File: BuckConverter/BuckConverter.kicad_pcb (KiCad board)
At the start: 2 copper layers, 130.3 x 135.9 mm, 43 parts, among them J1 Conn_01x01_Pin, J2 Conn_01x01_Pin, J3 Conn_01x01_Pin, J4 Conn_01x01_Pin, J5 Conn_01x01_Pin, Q1 IRF540N, U1 LM358, U2 LAUNCHXL-F28379D, U3 UCC5304DWVR, U4 TMV 0512SHI

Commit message: LPF updates
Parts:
- R1: value 10000 -> 10k
- R2, R3: value ? -> 500; footprint Resistor_SMD:R_0805_2012Metric -> Resistor_SMD:R_0603_1608Metric
- R4: value ? -> 10k
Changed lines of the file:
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@@
 		(tags "resistor")
 		(property "Reference" "R4"
-			(at 2.794 0 0)
+			(at 0 -1.65 180)
 			(layer "F.SilkS")
 			(effects
@@
 			)
 		)
-		(property "Value" "?"
-			(at 0 1.65 0)
+		(property "Value" "10k"
+			(at 0 1.65 180)
 			(layer "F.Fab")
 			(effects
@@
 		)
 		(fp_text user "${REFERENCE}"
-			(at 0 0 0)
+			(at 0 0 180)
 			(layer "F.Fab")
 			(effects
@@
 			)
 		)
-		(property "Value" "10000"
+		(property "Value" "10k"
 			(at 0 1.65 0)
 			(layer "F.Fab")
@@
 		)
 	)
-	(footprint "Resistor_SMD:R_0805_2012Metric"
+	(footprint "Resistor_SMD:R_0603_1608Metric"
 		(layer "F.Cu")
 		(at 147.392 112.756)
-		(descr "Resistor SMD 0805 (2012 Metric), square (rectangular) end terminal, IPC_7351 nominal, (Body size source: IPC-SM-782 page 72, https://www.pcb-3d.com/wordpress/wp-content/uploads/ipc-sm-782a_amendment_1_and_2.pdf), generated with kicad-footprint-generator")
+		(descr "Resistor SMD 0603 (1608 Metric), square (rectangular) end terminal, IPC_7351 nominal, (Body size source: IPC-SM-782 page 72, https://www.pcb-3d.com/wordpress/wp-content/uploads/ipc-sm-782a_amendment_1_and_2.pdf), generated with kicad-footprint-generator")
 		(tags "resistor")
 		(property "Reference" "R2"
-			(at 2.794 0 0)
+			(at 0 -1.43 0)
 			(layer "F.SilkS")
 			(effects
@@
 			)
 		)
-		(property "Value" "?"
-			(at 0 1.65 0)
+		(property "Value" "500"
+			(at 0 1.43 0)
 			(layer "F.Fab")
 			(effects
@@
 			)
 		)
-		(property "Footprint" "Resistor_SMD:R_0805_2012Metric"
+		(property "Footprint" "Resistor_SMD:R_0603_1608Metric"
 			(at 0 0 0)
 			(unlocked yes)
@@
 			)
 		)
-		(property "Part Number" "RMCF0805FT10K0"
+		(property "Part Number" "RT0603BRC07500RL"
 			(at 0 0 0)
 			(unlocked yes)
@@
 		(attr smd)
 		(fp_line
-			(start -0.227064 -0.735)
-			(end 0.227064 -0.735)
+			(start -0.237258 -0.5225)
+			(end 0.237258 -0.5225)
 			(stroke
 				(width 0.12)
@@
 		)
 		(fp_line
-			(start -0.227064 0.735)
-			(end 0.227064 0.735)
+			(start -0.237258 0.5225)
+			(end 0.237258 0.5225)
 			(stroke
 				(width 0.12)
@@
 		)
 		(fp_line
-			(start -1.68 -0.95)
-			(end 1.68 -0.95)
+			(start -1.48 -0.73)
+			(end 1.48 -0.73)
 			(stroke
 				(width 0.05)
@@
 		)
 		(fp_line
-			(start -1.68 0.95)
-			(end -1.68 -0.95)
+			(start -1.48 0.73)
+			(end -1.48 -0.73)
 			(stroke
 				(width 0.05)
@@
 		)
 		(fp_line
-			(start 1.68 -0.95)
-			(end 1.68 0.95)
+			(start 1.48 -0.73)
+			(end 1.48 0.73)
 			(stroke
 				(width 0.05)
@@
 		)
 		(fp_line
-			(start 1.68 0.95)
-			(end -1.68 0.95)
+			(start 1.48 0.73)
+			(end -1.48 0.73)
 			(stroke
 				(width 0.05)
@@
 		)
 		(fp_line
-			(start -1 -0.625)
-			(end 1 -0.625)
+			(start -0.8 -0.4125)
+			(end 0.8 -0.4125)
 			(stroke
 				(width 0.1)
@@
 		)
 		(fp_line
-			(start -1 0.625)
-			(end -1 -0.625)
+			(start -0.8 0.4125)
+			(end -0.8 -0.4125)
 			(stroke
 				(width 0.1)
@@
 		)
 		(fp_line
-			(start 1 -0.625)
-			(end 1 0.625)
+			(start 0.8 -0.4125)
+			(end 0.8 0.4125)
 			(stroke
 				(width 0.1)
@@
 		)
 		(fp_line
-			(start 1 0.625)
-			(end -1 0.625)
+			(start 0.8 0.4125)
+			(end -0.8 0.4125)
 			(stroke
 				(width 0.1)
@@
 			(effects
 				(font
-					(size 0.5 0.5)
-					(thickness 0.08)
+					(size 0.4 0.4)
+					(thickness 0.06)
 				)
 			)
 		)
 		(pad "1" smd roundrect
-			(at -0.9125 0)
-			(size 1.025 1.4)
+			(at -0.825 0)
+			(size 0.8 0.95)
 			(layers "F.Cu" "F.Paste" "F.Mask")
-			(roundrect_rratio 0.243902)
+			(roundrect_rratio 0.25)
 			(net 2 "Net-(U1A--)")
 			(pintype "passive")
 		)
 		(pad "2" smd roundrect
-			(at 0.9125 0)
-			(size 1.025 1.4)
+			(at 0.825 0)
+			(size 0.8 0.95)
 			(layers "F.Cu" "F.Paste" "F.Mask")
-			(roundrect_rratio 0.243902)
+			(roundrect_rratio 0.25)
 			(net 6 "/LPF/VFLIT")
 			(pintype "passive")
 		)
-		(model "${KICAD8_3DMODEL_DIR}/Resistor_SMD.3dshapes/R_0805_2012Metric.wrl"
+		(model "${KICAD8_3DMODEL_DIR}/Resistor_SMD.3dshapes/R_0603_1608Metric.wrl"
 			(offset
 				(xyz 0 0 0)
@@
 			)
 		)
-		(fp_text user "*"
-			(at -3.4163 -2.8956 0)
+		(fp_text user "${REFERENCE}"
+			(at 0 0 0)
+			(unlocked yes)
 			(layer "F.Fab")
 			(effects
@@
 			)
 		)
-		(fp_text user "${REFERENCE}"
-			(at 0 0 0)
-			(unlocked yes)
+		(fp_text user "*"
+			(at -3.4163 -2.8956 0)
 			(layer "F.Fab")
 			(effects
@@
 		(fp_text user "*"
 			(at -3.1196 0 0)
+			(unlocked yes)
 			(layer "F.SilkS")
 			(effects
@@
 		(fp_text user "*"
 			(at -3.1196 0 0)
-			(unlocked yes)
 			(layer "F.SilkS")
 			(effects
@@
 		(fp_text user "*"
 			(at -1.8496 0 0)
+			(unlocked yes)
 			(layer "F.Fab")
 			(effects
@@
 			)
 		)
-		(fp_text user "${REFERENCE}"
-			(at 7.65 2.075 0)
-			(unlocked yes)
+		(fp_text user "*"
+			(at -1.8496 0 0)
 			(layer "F.Fab")
 			(effects
@@
 			)
 		)
-		(fp_text user "*"
-			(at -1.8496 0 0)
+		(fp_text user "${REFERENCE}"
+			(at 7.65 2.075 0)
 			(unlocked yes)
 			(layer "F.Fab")
@@
 		)
 	)
-	(footprint "Resistor_SMD:R_0805_2012Metric"
+	(footprint "Resistor_SMD:R_0603_1608Metric"
 		(layer "F.Cu")
 		(at 147.392 105.898)
-		(descr "Resistor SMD 0805 (2012 Metric), square (rectangular) end terminal, IPC_7351 nominal, (Body size source: IPC-SM-782 page 72, https://www.pcb-3d.com/wordpress/wp-content/uploads/ipc-sm-782a_amendment_1_and_2.pdf), generated with kicad-footprint-generator")
+		(descr "Resistor SMD 0603 (1608 Metric), square (rectangular) end terminal, IPC_7351 nominal, (Body size source: IPC-SM-782 page 72, https://www.pcb-3d.com/wordpress/wp-content/uploads/ipc-sm-782a_amendment_1_and_2.pdf), generated with kicad-footprint-generator")
 		(tags "resistor")
 		(property "Reference" "R3"
-			(at 2.794 0 0)
+			(at 0 -1.43 0)
 			(layer "F.SilkS")
 			(effects
@@
 			)
 		)
-		(property "Value" "?"
-			(at 0 1.65 0)
+		(property "Value" "500"
+			(at 0 1.43 0)
 			(layer "F.Fab")
 			(effects
@@
 			)
 		)
-		(property "Footprint" "Resistor_SMD:R_0805_2012Metric"
+		(property "Footprint" "Resistor_SMD:R_0603_1608Metric"
 			(at 0 0 0)
 			(unlocked yes)
@@
 			)
 		)
-		(property "Part Number" "RMCF0805FT10K0"
+		(property "Part Number" "RT0603BRC07500RL"
 			(at 0 0 0)
 			(unlocked yes)
@@
 		(attr smd)
 		(fp_line
-			(start -0.227064 -0.735)
-			(end 0.227064 -0.735)
+			(start -0.237258 -0.5225)
+			(end 0.237258 -0.5225)
 			(stroke
 				(width 0.12)
@@
 		)
 		(fp_line
-			(start -0.227064 0.735)
-			(end 0.227064 0.735)
+			(start -0.237258 0.5225)
+			(end 0.237258 0.5225)
 			(stroke
 				(width 0.12)
@@
 		)
 		(fp_line
-			(start -1.68 -0.95)
-			(end 1.68 -0.95)
+			(start -1.48 -0.73)
+			(end 1.48 -0.73)
 			(stroke
 				(width 0.05)
@@
 		)
 		(fp_line
-			(start -1.68 0.95)
-			(end -1.68 -0.95)
+			(start -1.48 0.73)
+			(end -1.48 -0.73)
 			(stroke
 				(width 0.05)
@@
 		)
 		(fp_line
-			(start 1.68 -0.95)
-			(end 1.68 0.95)
+			(start 1.48 -0.73)
+			(end 1.48 0.73)
 			(stroke
 				(width 0.05)
@@
 		)
 		(fp_line
-			(start 1.68 0.95)
-			(end -1.68 0.95)
+			(start 1.48 0.73)
+			(end -1.48 0.73)
 			(stroke
 				(width 0.05)
@@
 		)
 		(fp_line
-			(start -1 -0.625)
-			(end 1 -0.625)
+			(start -0.8 -0.4125)
+			(end 0.8 -0.4125)
 			(stroke
 				(width 0.1)
@@
 		)
 		(fp_line
-			(start -1 0.625)
-			(end -1 -0.625)
+			(start -0.8 0.4125)
+			(end -0.8 -0.4125)
 			(stroke
 				(width 0.1)
@@
 		)
 		(fp_line
-			(start 1 -0.625)
-			(end 1 0.625)
+			(start 0.8 -0.4125)
+			(end 0.8 0.4125)
 			(stroke
 				(width 0.1)
@@
 		)
 		(fp_line
-			(start 1 0.625)
-			(end -1 0.625)
+			(start 0.8 0.4125)
+			(end -0.8 0.4125)
 			(stroke
 				(width 0.1)
@@
 			(effects
 				(font
-					(size 0.5 0.5)
-					(thickness 0.08)
+					(size 0.4 0.4)
+					(thickness 0.06)
 				)
 			)
 		)
 		(pad "1" smd roundrect
-			(at -0.9125 0)
-			(size 1.025 1.4)
+			(at -0.825 0)
+			(size 0.8 0.95)
 			(layers "F.Cu" "F.Paste" "F.Mask")
-			(roundrect_rratio 0.243902)
+			(roundrect_rratio 0.25)
 			(net 4 "Net-(U1A-+)")
 			(pintype "passive")
 		)
 		(pad "2" smd roundrect
-			(at 0.9125 0)
-			(size 1.025 1.4)
+			(at 0.825 0)
+			(size 0.8 0.95)
 			(layers "F.Cu" "F.Paste" "F.Mask")
-			(roundrect_rratio 0.243902)
+			(roundrect_rratio 0.25)
 			(net 1 "GND")
 			(pintype "passive")
 		)
-		(model "${KICAD8_3DMODEL_DIR}/Resistor_SMD.3dshapes/R_0805_2012Metric.wrl"
+		(model "${KICAD8_3DMODEL_DIR}/Resistor_SMD.3dshapes/R_0603_1608Metric.wrl"
 			(offset
 				(xyz 0 0 0)

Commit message: pcb name printed
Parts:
- added G***: LOGO, uwinengineeringlogo:uwinengilogo, F.Cu at (54.0, 59.9)
- added G***: LOGO, Totoro:Totoro, F.Cu at (63.2, 67.6)
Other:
- board text added: "Studio Buck Converter v0 - 24 Feb 2025 Steven Fung Andrew Nguyen Yanis Belassel"

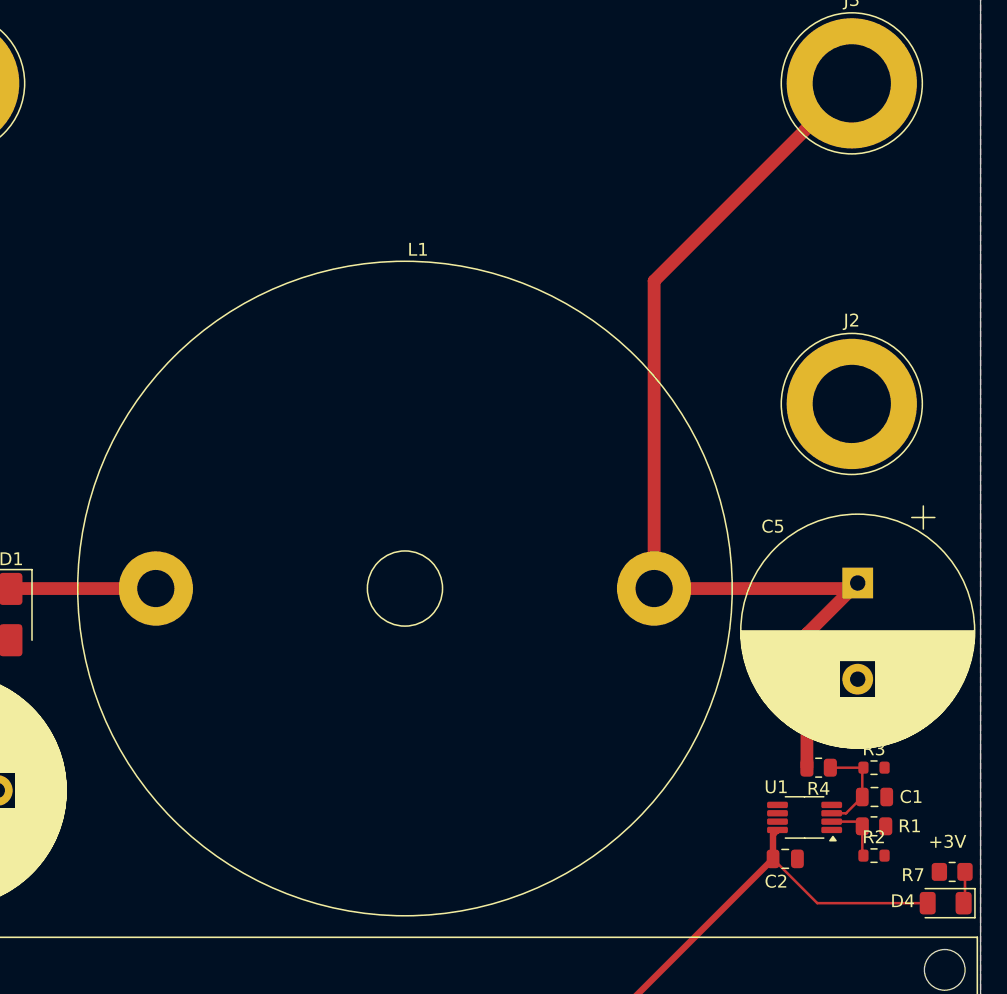
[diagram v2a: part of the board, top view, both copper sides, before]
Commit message: PCB updated LC footprints
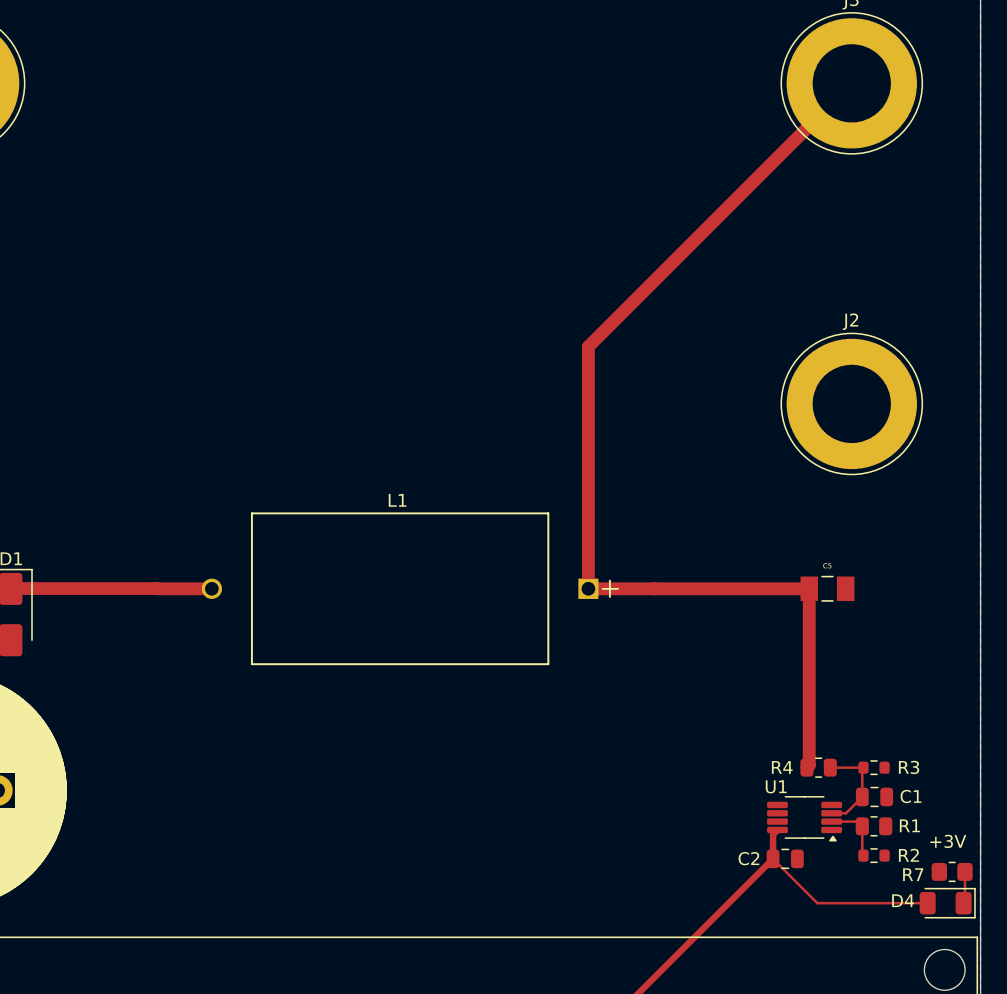
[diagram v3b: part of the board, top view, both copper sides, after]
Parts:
- C1: value C -> 22u
- C2: value C -> 1u
- C5: value ? -> GRM31CC72A475KE11L; footprint Capacitor_THT:CP_Radial_D18.0mm_P7.50mm -> GRM31CC72A475KE11L:CAPC3216X190N
- L1: value ? -> 5900-333-RC; footprint Inductor_THT:L_Radial_D50.8mm_P38.86mm_Vishay_IHB-6 -> 5900-333-RC:IND_BOURNS_5900
- moved L1 33.7 mm to (125.1, 91.9), turned to 180 degrees
- moved C5 2.40 mm to (143.8, 91.9), turned to 0 degrees
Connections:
- L1 pad 1: /VSW -> /VOUT
- L1 pad 2: /VOUT -> /VSW
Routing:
- net /VSW: track 136.3 -> 140.3 mm
- net /VOUT: track 77.9 -> 79.2 mm

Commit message: PCB Final Draft
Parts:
- C9: value C -> 33p; footprint Resistor_SMD:R_0805_2012Metric_Pad1.20x1.40mm_HandSolder -> 600F330FT250XT:CAP_600F0R1AT250T_ATC
- R9: value R -> 51; footprint Resistor_SMD:R_0805_2012Metric_Pad1.20x1.40mm_HandSolder -> RC0805FR_0751RL:RC0805N_YAG
- moved C9 0.52 mm to (33.3, 97.3)
- moved R9 0.18 mm to (30.0, 96.8)
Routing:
- net /LPF/VFLIT: track 0.00 -> 9.03 mm

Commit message: Update PCB and BOM
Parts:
- added REF**: MountingHole_2.2mm_M2_DIN965_Pad, MountingHole:MountingHole_2.2mm_M2_DIN965_Pad, F.Cu at (159.5, 181.0)
- added REF**: MountingHole_2.2mm_M2_DIN965_Pad, MountingHole:MountingHole_2.2mm_M2_DIN965_Pad, F.Cu at (22.0, 39.5)
- added REF**: MountingHole_2.2mm_M2_DIN965_Pad, MountingHole:MountingHole_2.2mm_M2_DIN965_Pad, F.Cu at (159.0, 39.5)
- added REF**: MountingHole_2.2mm_M2_DIN965_Pad, MountingHole:MountingHole_2.2mm_M2_DIN965_Pad, F.Cu at (22.0, 181.0)
- C5: value GRM31CC72A475KE11L -> 4.7 µF
- L1: value 5900-333-RC -> 33mH
- R10: value 7R -> 7
- R11: value 12R -> 12
- R12: value 50R -> 50
- U1: value LM358 -> LM358AP; footprint Package_SO:VSSOP-8_3x3mm_P0.65mm -> LM358AP:P8
- moved U1 12.0 mm to (130.6, 106.2)
- moved C2 10.0 mm to (131.6, 117.6)
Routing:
- net Net-(U1-1IN-): track 4.83 -> 11.4 mm
- net Net-(U1-1IN+): track 7.69 -> 12.2 mm
- net /LPF/VFLIT: track 9.03 -> 12.0 mm
- net +3.3V: track 36.9 -> 39.8 mm
- net /PWM: track 87.2 -> 85.4 mm
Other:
- board size 130.3 x 135.9 mm -> 145.5 x 149.6 mm
